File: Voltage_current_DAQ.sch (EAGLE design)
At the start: 26 parts, among them IC1 INA128U

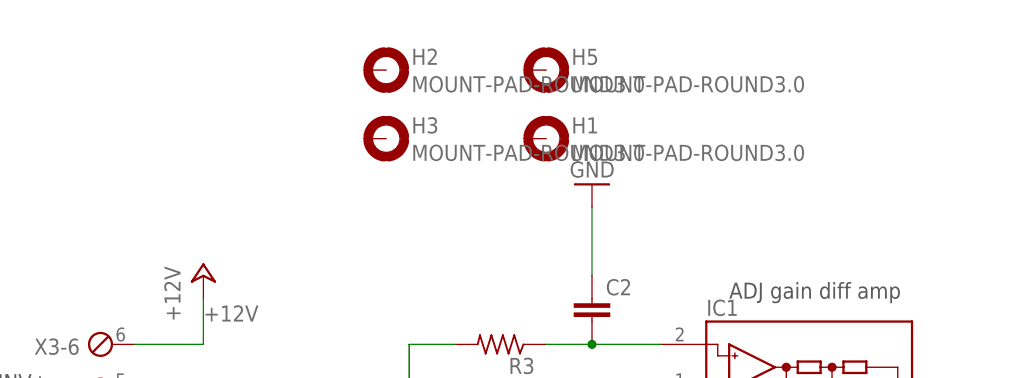
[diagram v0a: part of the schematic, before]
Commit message: gerbers generated sent to OSHpark
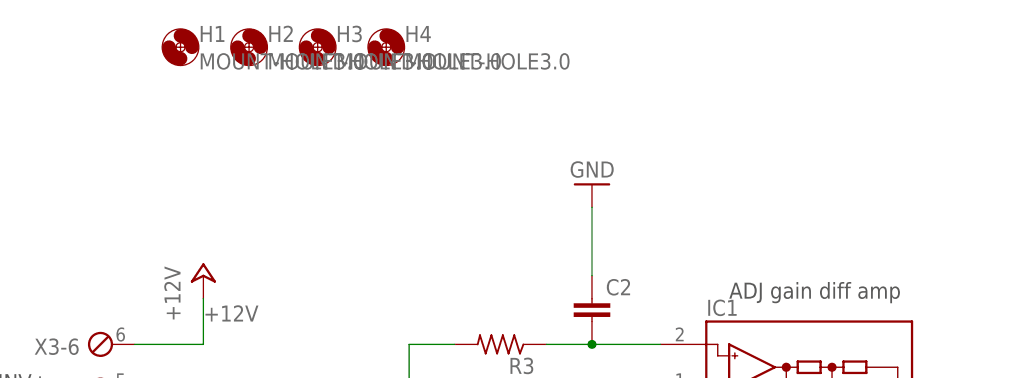
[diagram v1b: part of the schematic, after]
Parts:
- removed H5: MOUNT-PAD-ROUND3.0, holes:MOUNT-PAD-ROUND3.0
- added H4: MOUNT-HOLE3.0, holes:MOUNT-HOLE3.0
- H1, H2, H3: value MOUNT-PAD-ROUND3.0 -> MOUNT-HOLE3.0; device holes:MOUNT-PAD-ROUND3.0 -> holes:MOUNT-HOLE3.0
- R1, R3, R4, R7, R9: device rcl:R-US_R0603 -> rcl:R-US_R0805
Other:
- moved on the sheet: H1, H2, H3
